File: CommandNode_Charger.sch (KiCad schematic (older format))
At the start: 0 parts

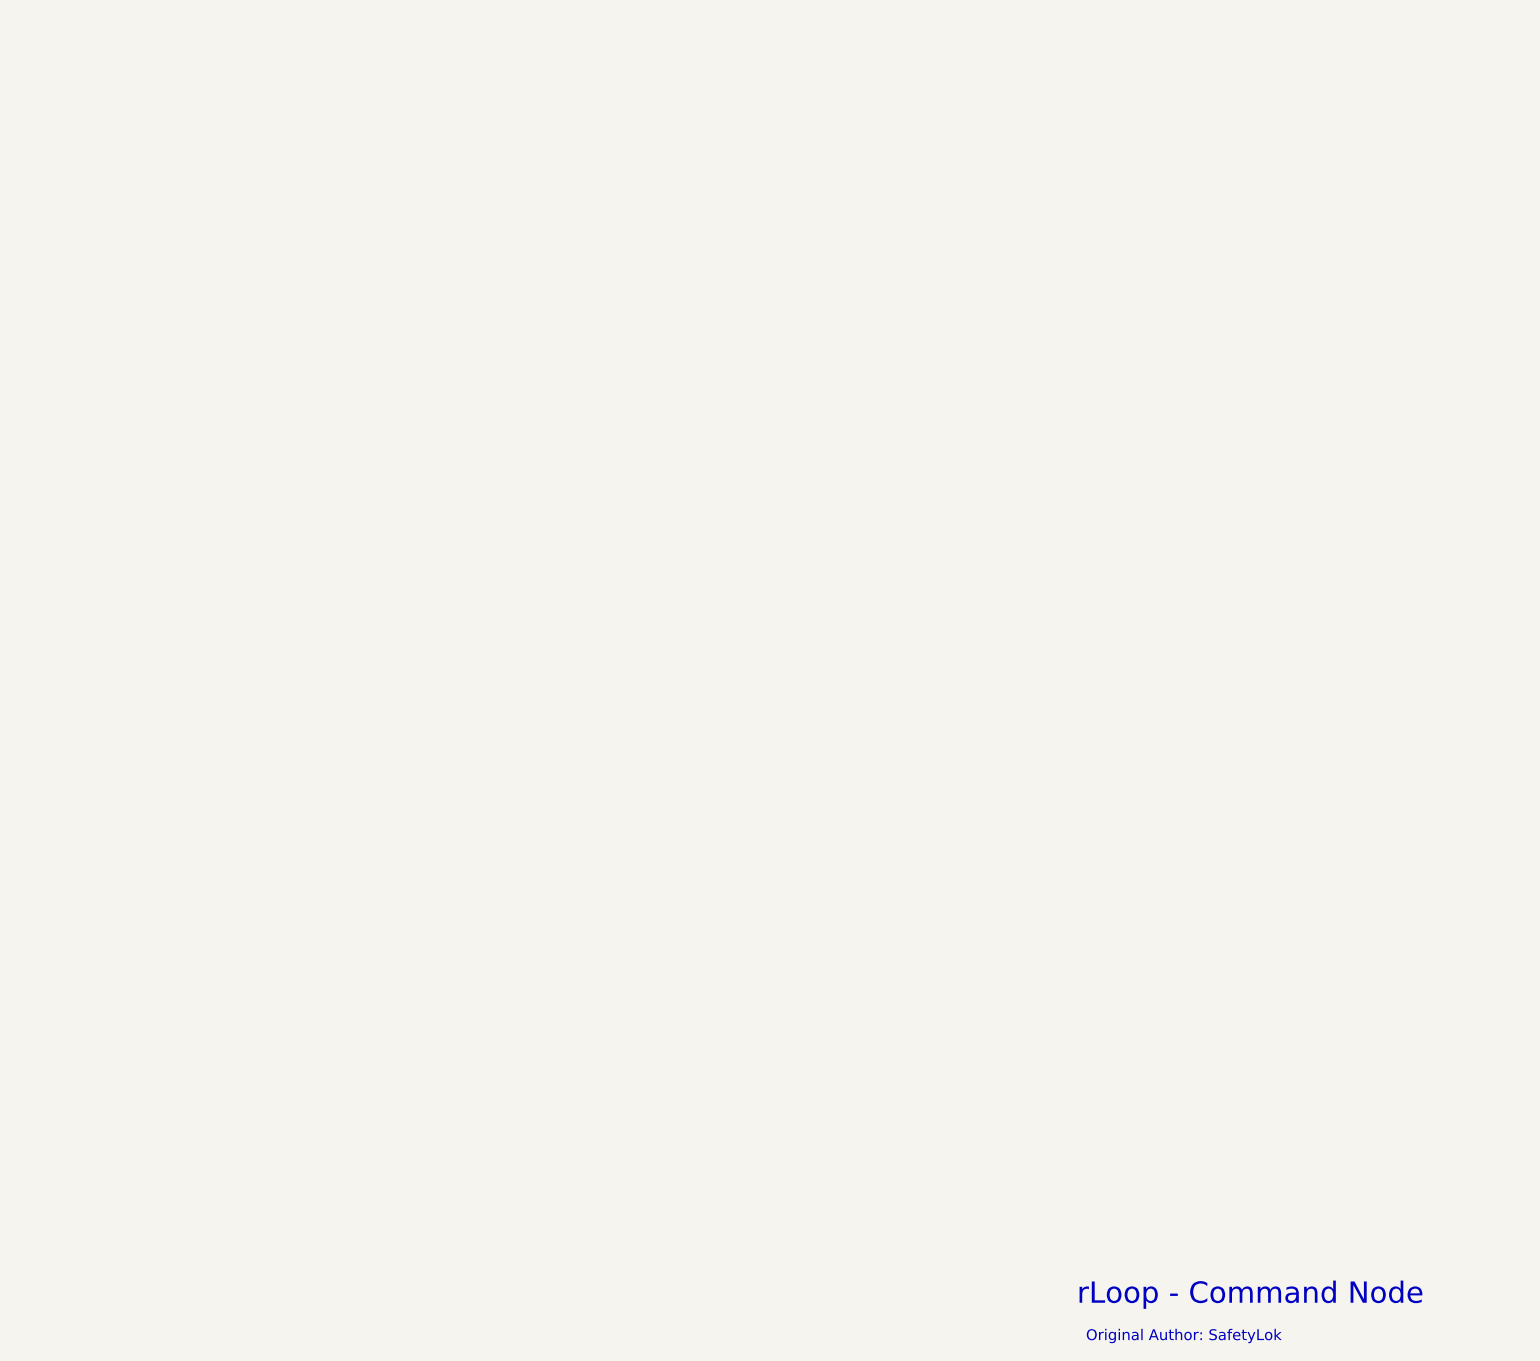
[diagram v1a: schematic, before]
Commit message: Update charger control interface
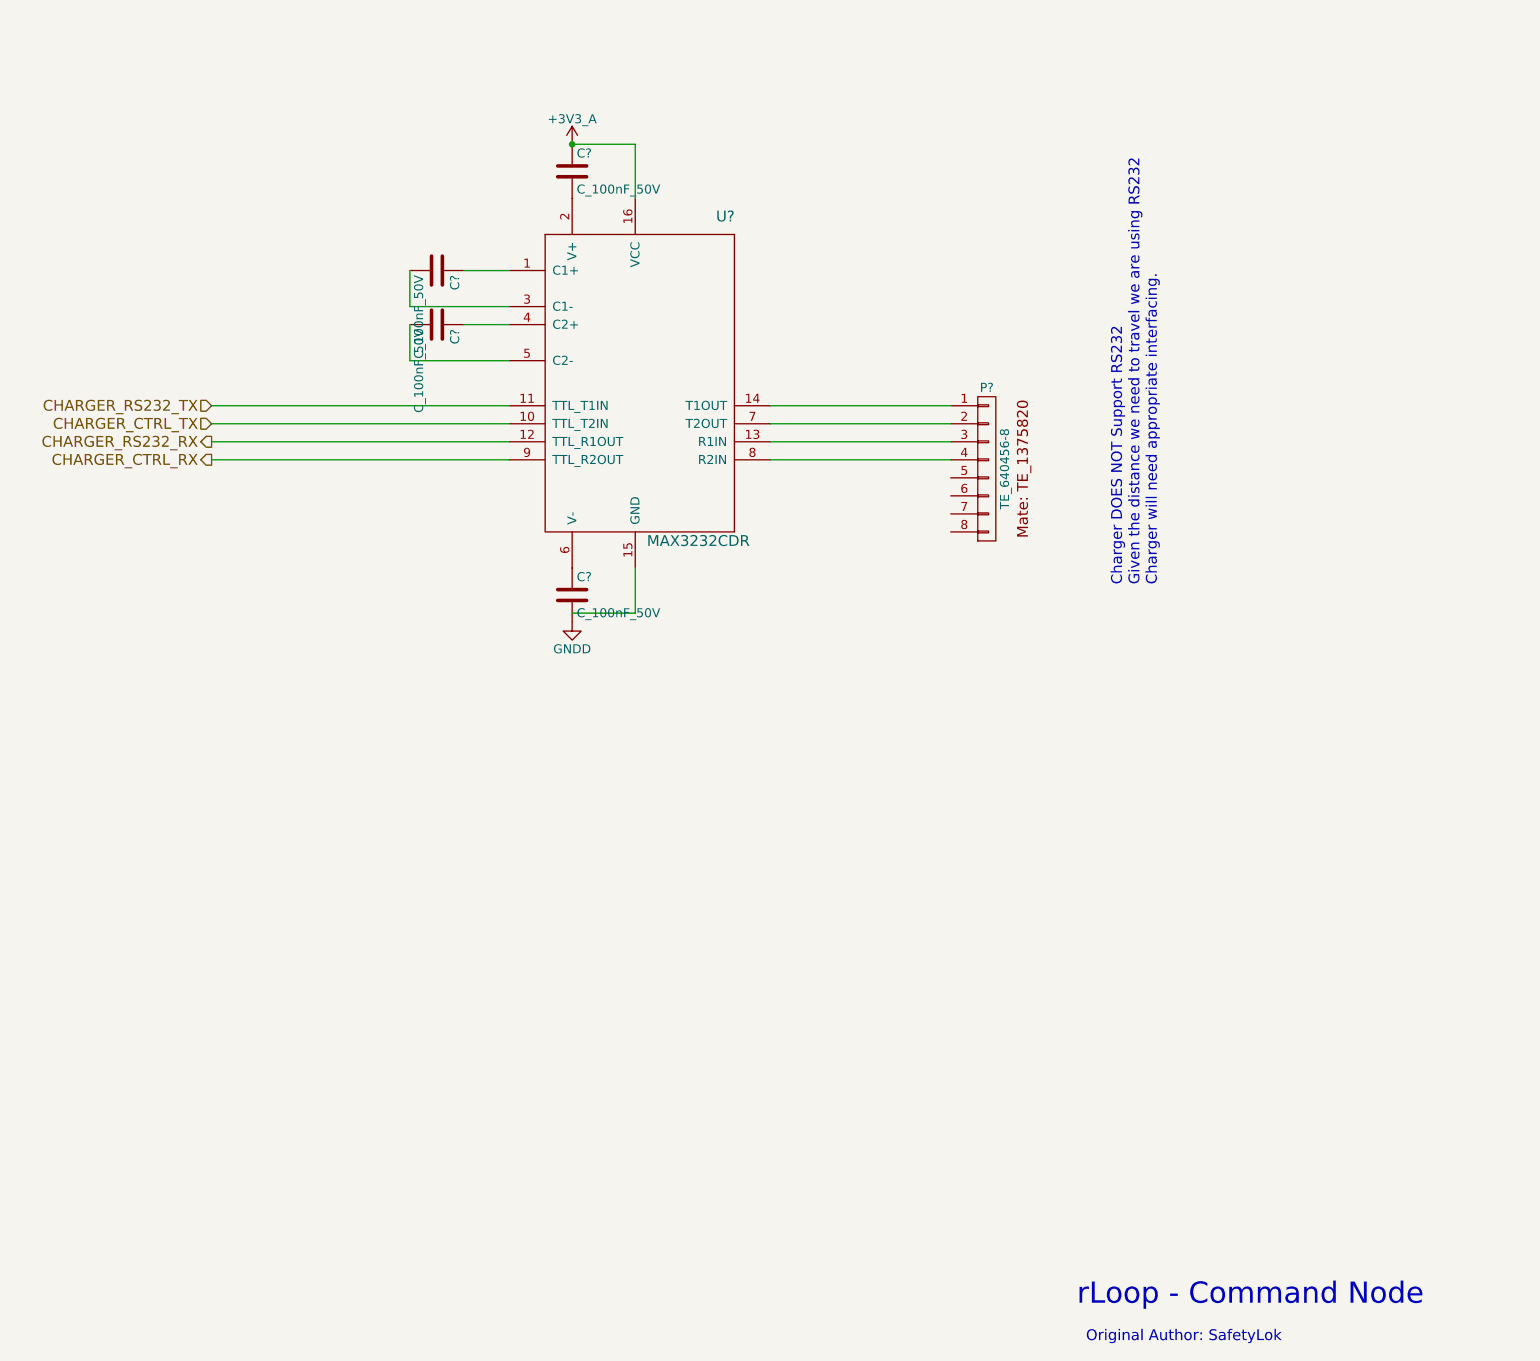
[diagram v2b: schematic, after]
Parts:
- added C? (x4): C_100nF_50V, RLOOP_FOOTPRINTS:rLoop_C_0603, symbol C_100nF_50V
- added P?: TE_640456-8, RLOOP_FOOTPRINTS:rLoop_TE640456-8, symbol TE_640456-8
- added U?: MAX3232CDR, RLOOP_FOOTPRINTS:rLoop_SOIC_16, symbol MAX3232CDR
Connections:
- net labels added: +3V3_A, CHARGER_CTRL_RX, CHARGER_CTRL_TX, CHARGER_RS232_RX, CHARGER_RS232_TX, GNDD
- wire segments 0 -> 18
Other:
- note added: "Charger DOES NOT Support RS232\nGiven the distance we need to travel we are using RS232\nCharger will need appropriate interfacing."
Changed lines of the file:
@@
 Text Notes 11950 10400 0    60   ~ 0
 Original Author: SafetyLok
+$Comp
+L MAX3232CDR U?
+U 1 1 575CEC05
+P 8950 4250
+F 0 "U?" H 9950 4350 60  0000 C CNN
+F 1 "MAX3232CDR" H 9800 2550 60  0000 C CNN
+F 2 "RLOOP_FOOTPRINTS:rLoop_SOIC_16" H 9150 3650 60  0001 C CNN
+F 3 "" H 9150 3650 60  0000 C CNN
+	1    8950 4250
+	1    0    0    -1
+$EndComp
+$Comp
+L C_100nF_50V C?
+U 1 1 575CEC80
+P 9100 3900
+F 0 "C?" H 9125 4000 50  0000 L CNN
+F 1 "C_100nF_50V" H 9125 3800 50  0000 L CNN
+F 2 "RLOOP_FOOTPRINTS:rLoop_C_0603" H 9138 3750 50  0001 C CNN
+F 3 "" H 9100 3900 50  0000 C CNN
+	1    9100 3900
+	1    0    0    -1
+$EndComp
+$Comp
+L C_100nF_50V C?
+U 1 1 575CECE3
+P 9100 6250
+F 0 "C?" H 9125 6350 50  0000 L CNN
+F 1 "C_100nF_50V" H 9125 6150 50  0000 L CNN
+F 2 "RLOOP_FOOTPRINTS:rLoop_C_0603" H 9138 6100 50  0001 C CNN
+F 3 "" H 9100 6250 50  0000 C CNN
+	1    9100 6250
+	1    0    0    -1
+$EndComp
+$Comp
+L C_100nF_50V C?
+U 1 1 575CED70
+P 8350 4450
+F 0 "C?" H 8375 4550 50  0000 L CNN
+F 1 "C_100nF_50V" H 8375 4350 50  0000 L CNN
+F 2 "RLOOP_FOOTPRINTS:rLoop_C_0603" H 8388 4300 50  0001 C CNN
+F 3 "" H 8350 4450 50  0000 C CNN
+	1    8350 4450
+	0    1    1    0
+$EndComp
+$Comp
+L C_100nF_50V C?
+U 1 1 575CEDE1
+P 8350 4750
+F 0 "C?" H 8375 4850 50  0000 L CNN
+F 1 "C_100nF_50V" H 8375 4650 50  0000 L CNN
+F 2 "RLOOP_FOOTPRINTS:rLoop_C_0603" H 8388 4600 50  0001 C CNN
+F 3 "" H 8350 4750 50  0000 C CNN
+	1    8350 4750
+	0    1    1    0
+$EndComp
+$Comp
+L +3V3_A #PWR?
+U 1 1 575CEDEE
+P 9100 3750
+F 0 "#PWR?" H 9100 3600 50  0001 C CNN
+F 1 "+3V3_A" H 9100 3890 50  0000 C CNN
+F 2 "" H 9100 3750 60  0000 C CNN
+F 3 "" H 9100 3750 60  0000 C CNN
+	1    9100 3750
+	1    0    0    -1
+$EndComp
+Wire Wire Line
+	9450 4050 9450 3750
+Wire Wire Line
+	9450 3750 9100 3750
+Connection ~ 9100 3750
+$Comp
+L GNDD #PWR?
+U 1 1 575CEE15
+P 9100 6400
+F 0 "#PWR?" H 9100 6150 50  0001 C CNN
+F 1 "GNDD" H 9100 6250 50  0000 C CNN
+F 2 "" H 9100 6400 50  0000 C CNN
+F 3 "" H 9100 6400 50  0000 C CNN
+	1    9100 6400
+	1    0    0    -1
+$EndComp
+Wire Wire Line
+	9100 6350 9450 6350
+Wire Wire Line
+	9450 6350 9450 6100
+Wire Wire Line
+	8750 4450 8500 4450
+Wire Wire Line
+	8750 4650 8200 4650
+Wire Wire Line
+	8200 4650 8200 4450
+Wire Wire Line
+	8750 4750 8500 4750
+Wire Wire Line
+	8200 4950 8750 4950
+Wire Wire Line
+	8200 4950 8200 4750
+$Comp
+L TE_640456-8 P?
+U 1 1 575CEF1D
+P 11350 5150
+F 0 "P?" H 11400 5200 50  0000 C CNN
+F 1 "TE_640456-8" V 11500 4750 50  0000 C CNN
+F 2 "RLOOP_FOOTPRINTS:rLoop_TE640456-8" H 11400 4750 50  0001 C CNN
+F 3 "" H 11400 4750 50  0000 C CNN
+	1    11350 5150
+	1    0    0    -1
+$EndComp
+Wire Wire Line
+	10200 5200 11200 5200
+Wire Wire Line
+	11200 5300 10200 5300
+Wire Wire Line
+	10200 5400 11200 5400
+Wire Wire Line
+	10200 5500 11200 5500
+Text Notes 12350 6200 1    60   ~ 0
+Charger DOES NOT Support RS232\nGiven the distance we need to travel we are using RS232\nCharger will need appropriate interfacing.
+Wire Wire Line
+	8750 5200 7100 5200
+Wire Wire Line
+	8750 5400 7100 5400
+Wire Wire Line
+	8750 5300 7100 5300
+Wire Wire Line
+	7100 5500 8750 5500
+Text HLabel 7100 5300 0    60   Input ~ 0
+CHARGER_CTRL_TX
+Text HLabel 7100 5400 0    60   Output ~ 0
+CHARGER_RS232_RX
+Text HLabel 7100 5500 0    60   Output ~ 0
+CHARGER_CTRL_RX
+Text HLabel 7100 5200 0    60   Input ~ 0
+CHARGER_RS232_TX
 $EndSCHEMATC

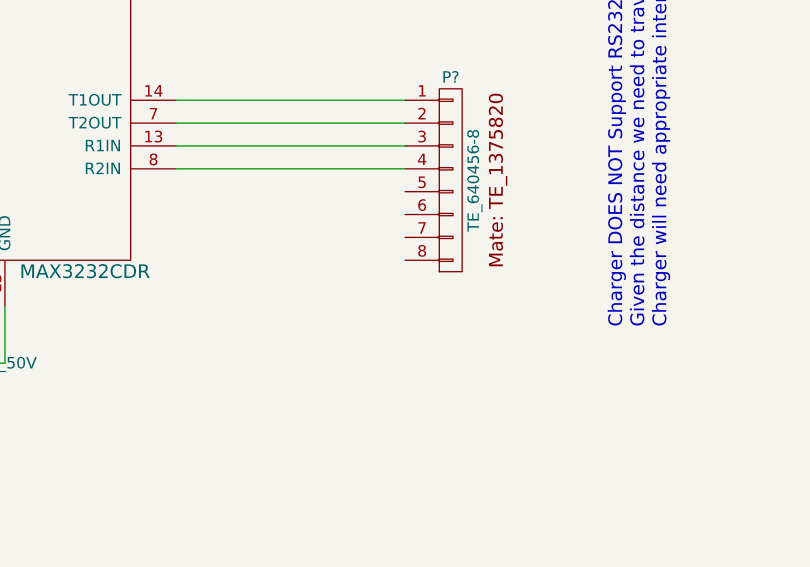
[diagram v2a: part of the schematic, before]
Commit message: Finish and print schematics for review
Lifting mechanism, charger interface, Data Enable on HE controller
RS585, Park Brake and node core.
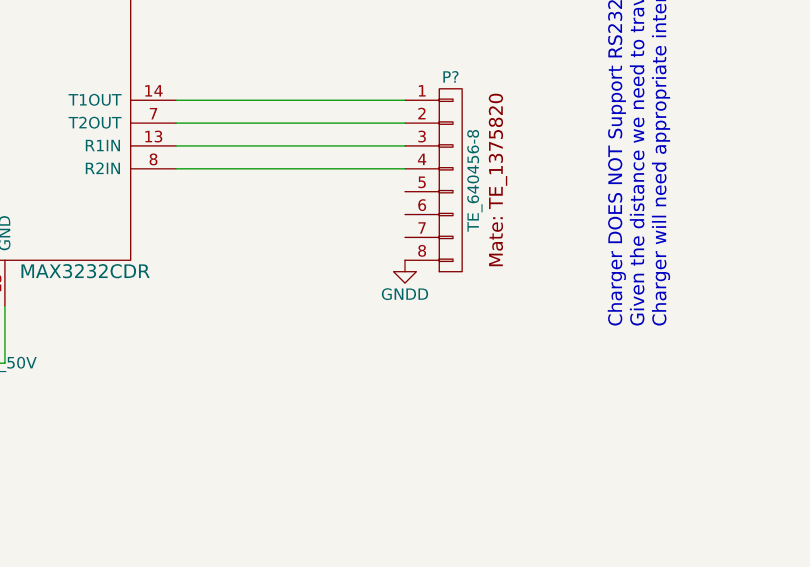
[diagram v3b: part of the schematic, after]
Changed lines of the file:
@@
 $Descr A3 16535 11693
 encoding utf-8
-Sheet 4 7
+Sheet 4 8
 Title "Battery Charger Interface"
 Date ""
@@
 Text HLabel 7100 5200 0    60   Input ~ 0
 CHARGER_RS232_TX
+$Comp
+L GNDD #PWR?
+U 1 1 576A2885
+P 11200 5900
+F 0 "#PWR?" H 11200 5650 50  0001 C CNN
+F 1 "GNDD" H 11200 5750 50  0000 C CNN
+F 2 "" H 11200 5900 50  0000 C CNN
+F 3 "" H 11200 5900 50  0000 C CNN
+	1    11200 5900
+	1    0    0    -1
+$EndComp
 $EndSCHEMATC
